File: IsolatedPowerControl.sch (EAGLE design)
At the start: 41 parts, among them Q1 FDN340P, Q2 FDN340P, U1 MCP23008-E/SO, U2 MCP4716A0T-E/CH, U3 MCP6273T-E/CH

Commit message: Another reroute!
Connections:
- net LOWSIDEONOFF_A: now also U1.GP7; no longer U1.GP1
- net V+: now also U1.GP1
- net V-: now also U1.GP5, U1.GP6
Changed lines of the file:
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@@
 <part name="R12" library="rcl" deviceset="R-EU_" device="R0603" value="10"/>
 <part name="P+9" library="supply1" deviceset="V+" device=""/>
-<part name="P-5" library="supply1" deviceset="V-" device=""/>
 <part name="U2" library="MCP4716A0T" deviceset="MCP4716A0T-E/CH" device=""/>
 <part name="P-6" library="supply1" deviceset="V-" device=""/>
@@
 <part name="R16" library="rcl" deviceset="R-EU_" device="R0805" value="10K"/>
 <part name="Q2" library="transistor-power" deviceset="FDN360P" device="" value="FDN340P"/>
+<part name="P-5" library="supply1" deviceset="V-" device=""/>
 </parts>
 <sheets>
@@
 <instance part="R12" gate="G$1" x="332.74" y="40.64" rot="R180"/>
 <instance part="P+9" gate="1" x="347.98" y="60.96"/>
-<instance part="P-5" gate="1" x="248.92" y="22.86"/>
 <instance part="U2" gate="A" x="213.36" y="-63.5"/>
 <instance part="P-6" gate="1" x="175.26" y="-81.28"/>
@@
 <instance part="R16" gate="G$1" x="340.36" y="12.7" rot="R90"/>
 <instance part="Q2" gate="G$1" x="345.44" y="2.54"/>
+<instance part="P-5" gate="1" x="248.92" y="-12.7"/>
 </instances>
 <busses>
@@
 <wire x1="248.92" y1="38.1" x2="248.92" y2="35.56" width="0.1524" layer="91"/>
 <pinref part="C2" gate="G$1" pin="1"/>
+<pinref part="U1" gate="A" pin="GP1"/>
+<wire x1="238.76" y1="5.08" x2="241.3" y2="5.08" width="0.1524" layer="91"/>
+<wire x1="241.3" y1="5.08" x2="241.3" y2="22.86" width="0.1524" layer="91"/>
+<junction x="241.3" y="22.86"/>
 </segment>
 <segment>
@@
 </segment>
 <segment>
-<pinref part="P-5" gate="1" pin="V-"/>
-<wire x1="248.92" y1="27.94" x2="248.92" y2="25.4" width="0.1524" layer="91"/>
-<pinref part="C2" gate="G$1" pin="2"/>
-</segment>
-<segment>
 <pinref part="U2" gate="A" pin="VSS"/>
 <wire x1="195.58" y1="-73.66" x2="175.26" y2="-73.66" width="0.1524" layer="91"/>
@@
 <wire x1="248.92" y1="-73.66" x2="248.92" y2="-76.2" width="0.1524" layer="91"/>
 <pinref part="P-10" gate="1" pin="V-"/>
+</segment>
+<segment>
+<pinref part="C2" gate="G$1" pin="2"/>
+<pinref part="U1" gate="A" pin="GP6"/>
+<wire x1="238.76" y1="17.78" x2="248.92" y2="17.78" width="0.1524" layer="91"/>
+<wire x1="248.92" y1="17.78" x2="248.92" y2="15.24" width="0.1524" layer="91"/>
+<pinref part="U1" gate="A" pin="GP5"/>
+<wire x1="248.92" y1="15.24" x2="238.76" y2="15.24" width="0.1524" layer="91"/>
+<wire x1="248.92" y1="15.24" x2="248.92" y2="-10.16" width="0.1524" layer="91"/>
+<junction x="248.92" y="15.24"/>
+<wire x1="248.92" y1="27.94" x2="248.92" y2="17.78" width="0.1524" layer="91"/>
+<junction x="248.92" y="17.78"/>
+<pinref part="P-5" gate="1" pin="V-"/>
 </segment>
 </net>
@@
 <net name="LOWSIDEONOFF_A" class="0">
 <segment>
-<pinref part="U1" gate="A" pin="GP1"/>
-<wire x1="238.76" y1="5.08" x2="269.24" y2="5.08" width="0.1524" layer="91"/>
-<label x="254" y="5.08" size="1.778" layer="95"/>
-</segment>
-<segment>
 <wire x1="302.26" y1="-22.86" x2="327.66" y2="-22.86" width="0.1524" layer="91"/>
 <label x="302.26" y="-22.86" size="1.778" layer="95"/>
 <pinref part="R11" gate="G$1" pin="1"/>
 </segment>
-</net>
+<segment>
+<pinref part="U1" gate="A" pin="GP7"/>
+<wire x1="238.76" y1="20.32" x2="269.24" y2="20.32" width="0.1524" layer="91"/>
+<label x="254" y="20.32" size="1.778" layer="95"/>
+</segment>
+</net>

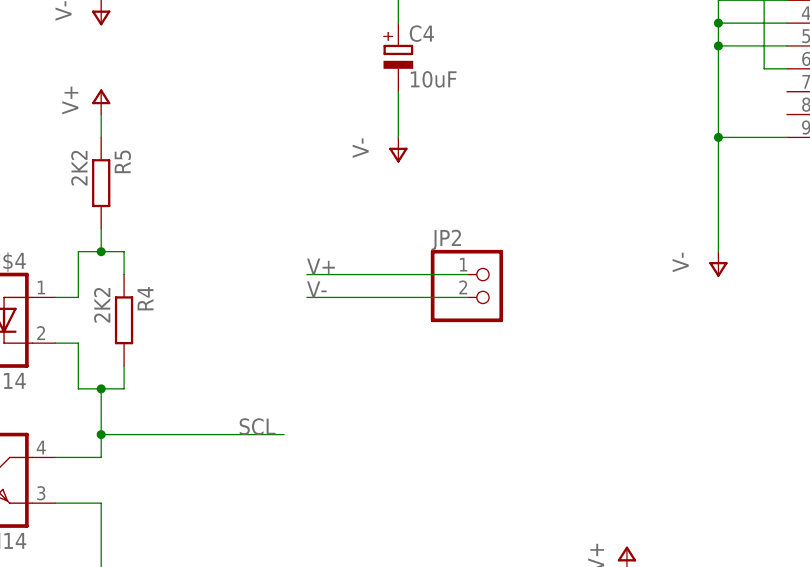
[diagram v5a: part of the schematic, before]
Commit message: Tweaks following etching to open up clearances
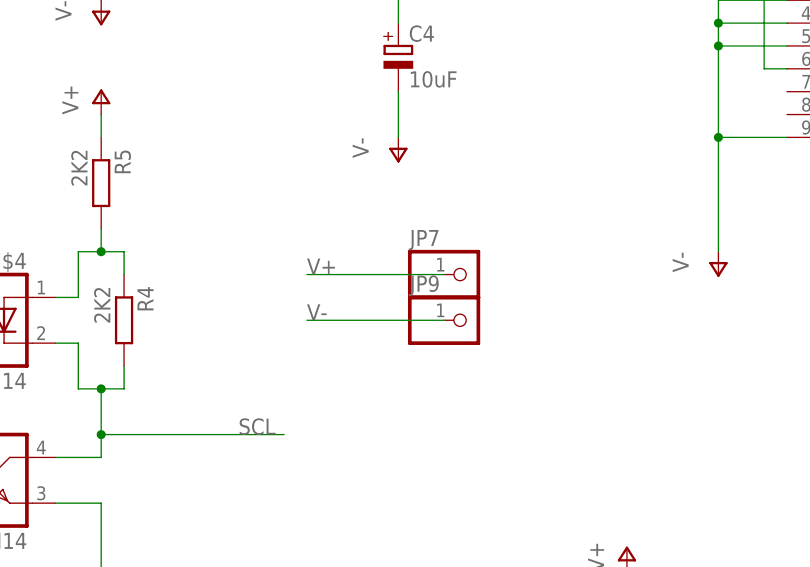
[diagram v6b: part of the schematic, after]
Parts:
- removed JP2: (no value), pinhead:PINHD-1X2
- added JP7, JP9: (no value), pinhead:PINHD-1X1LARGEPAD
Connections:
- net V+: now also JP7.1; no longer JP2.1
- net V-: now also JP9.1; no longer JP2.2
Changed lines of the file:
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@@
 <part name="GND5" library="supply1" deviceset="GND" device=""/>
 <part name="JP5" library="pinhead" deviceset="PINHD-1X4" device=""/>
-<part name="JP2" library="pinhead" deviceset="PINHD-1X2" device=""/>
 <part name="JP1" library="pinhead" deviceset="PINHD-1X1" device="LARGEPAD"/>
 <part name="JP3" library="pinhead" deviceset="PINHD-1X1" device="LARGEPAD"/>
@@
 <part name="Q2" library="transistor-power" deviceset="FDN360P" device="" value="FDN340P"/>
 <part name="P-5" library="supply1" deviceset="V-" device=""/>
+<part name="JP7" library="pinhead" deviceset="PINHD-1X1" device="LARGEPAD"/>
+<part name="JP9" library="pinhead" deviceset="PINHD-1X1" device="LARGEPAD"/>
 </parts>
 <sheets>
@@
 <instance part="GND5" gate="1" x="17.78" y="20.32"/>
 <instance part="JP5" gate="A" x="-88.9" y="12.7" rot="MR0"/>
-<instance part="JP2" gate="G$1" x="160.02" y="-15.24"/>
 <instance part="JP1" gate="G$1" x="449.58" y="25.4"/>
 <instance part="JP3" gate="G$1" x="449.58" y="30.48"/>
@@
 <instance part="Q2" gate="G$1" x="345.44" y="2.54"/>
 <instance part="P-5" gate="1" x="248.92" y="-12.7"/>
+<instance part="JP7" gate="G$1" x="157.48" y="-12.7"/>
+<instance part="JP9" gate="G$1" x="157.48" y="-17.78"/>
 </instances>
 <busses>
@@
 </segment>
 <segment>
-<wire x1="157.48" y1="-12.7" x2="139.7" y2="-12.7" width="0.1524" layer="91"/>
+<wire x1="154.94" y1="-12.7" x2="139.7" y2="-12.7" width="0.1524" layer="91"/>
 <label x="139.7" y="-12.7" size="1.778" layer="95"/>
-<pinref part="JP2" gate="G$1" pin="1"/>
+<pinref part="JP7" gate="G$1" pin="1"/>
 </segment>
 <segment>
@@
 </segment>
 <segment>
-<wire x1="157.48" y1="-15.24" x2="139.7" y2="-15.24" width="0.1524" layer="91"/>
-<label x="139.7" y="-15.24" size="1.778" layer="95"/>
-<pinref part="JP2" gate="G$1" pin="2"/>
-</segment>
-<segment>
+<wire x1="154.94" y1="-17.78" x2="139.7" y2="-17.78" width="0.1524" layer="91"/>
+<label x="139.7" y="-17.78" size="1.778" layer="95"/>
+<pinref part="JP9" gate="G$1" pin="1"/>
+</segment>
+<segment>

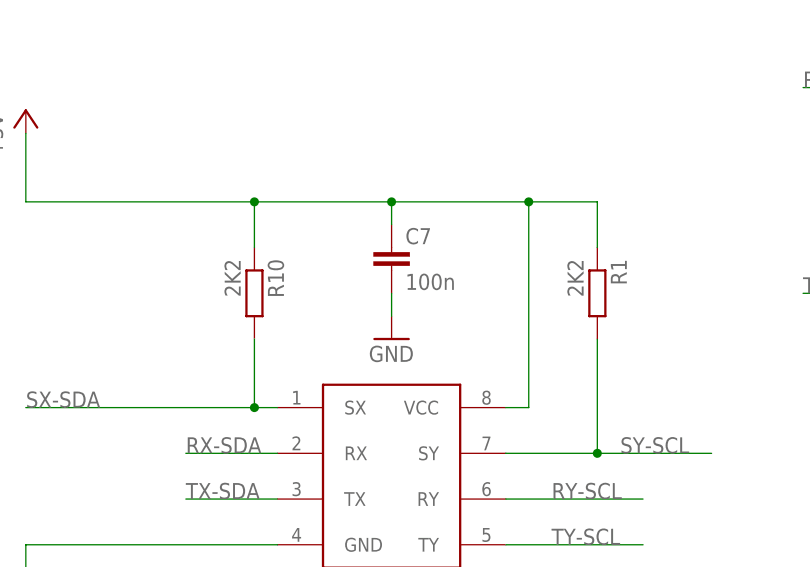
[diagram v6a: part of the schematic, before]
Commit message: Added test software
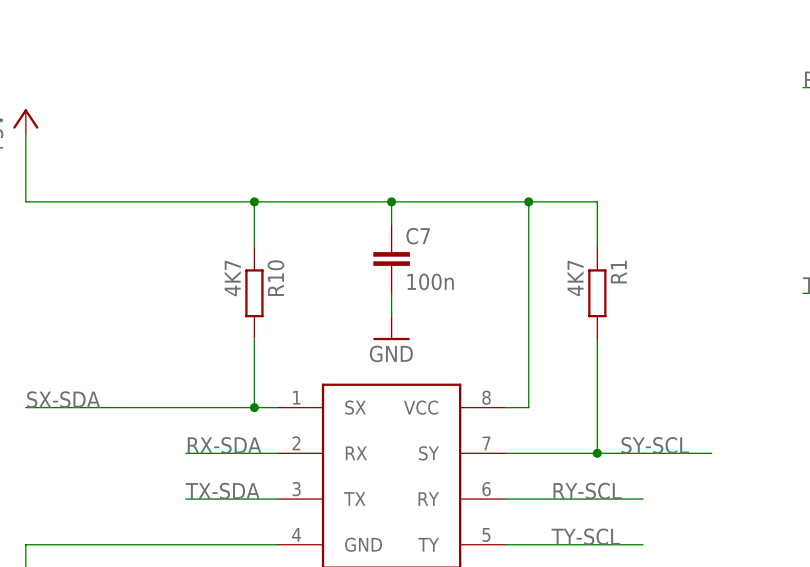
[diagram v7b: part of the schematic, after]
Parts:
- R1, R10: value 2K2 -> 4K7
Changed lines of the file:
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@@
 <grid distance="0.1" unitdist="inch" unit="inch" style="lines" multiple="1" display="no" altdistance="0.01" altunitdist="inch" altunit="inch"/>
 <layers>
-<layer number="1" name="Top" color="4" fill="1" visible="no" active="no"/>
-<layer number="2" name="Route2" color="1" fill="3" visible="no" active="no"/>
-<layer number="3" name="Route3" color="4" fill="3" visible="no" active="no"/>
-<layer number="14" name="Route14" color="1" fill="6" visible="no" active="no"/>
-<layer number="15" name="Route15" color="4" fill="6" visible="no" active="no"/>
-<layer number="16" name="Bottom" color="1" fill="1" visible="no" active="no"/>
-<layer number="17" name="Pads" color="2" fill="1" visible="no" active="no"/>
-<layer number="18" name="Vias" color="2" fill="1" visible="no" active="no"/>
-<layer number="19" name="Unrouted" color="6" fill="1" visible="no" active="no"/>
-<layer number="20" name="Dimension" color="15" fill="1" visible="no" active="no"/>
-<layer number="21" name="tPlace" color="7" fill="1" visible="no" active="no"/>
-<layer number="22" name="bPlace" color="7" fill="1" visible="no" active="no"/>
-<layer number="23" name="tOrigins" color="15" fill="1" visible="no" active="no"/>
-<layer number="24" name="bOrigins" color="15" fill="1" visible="no" active="no"/>
-<layer number="25" name="tNames" color="7" fill="1" visible="no" active="no"/>
-<layer number="26" name="bNames" color="7" fill="1" visible="no" active="no"/>
-<layer number="27" name="tValues" color="7" fill="1" visible="no" active="no"/>
-<layer number="28" name="bValues" color="7" fill="1" visible="no" active="no"/>
+<layer number="1" name="Top" color="4" fill="1" visible="yes" active="no"/>
+<layer number="2" name="Route2" color="1" fill="3" visible="yes" active="no"/>
+<layer number="3" name="Route3" color="4" fill="3" visible="yes" active="no"/>
+<layer number="14" name="Route14" color="1" fill="6" visible="yes" active="no"/>
+<layer number="15" name="Route15" color="4" fill="6" visible="yes" active="no"/>
+<layer number="16" name="Bottom" color="1" fill="1" visible="yes" active="no"/>
+<layer number="17" name="Pads" color="2" fill="1" visible="yes" active="no"/>
+<layer number="18" name="Vias" color="2" fill="1" visible="yes" active="no"/>
+<layer number="19" name="Unrouted" color="6" fill="1" visible="yes" active="no"/>
+<layer number="20" name="Dimension" color="15" fill="1" visible="yes" active="no"/>
+<layer number="21" name="tPlace" color="7" fill="1" visible="yes" active="no"/>
+<layer number="22" name="bPlace" color="7" fill="1" visible="yes" active="no"/>
+<layer number="23" name="tOrigins" color="15" fill="1" visible="yes" active="no"/>
+<layer number="24" name="bOrigins" color="15" fill="1" visible="yes" active="no"/>
+<layer number="25" name="tNames" color="7" fill="1" visible="yes" active="no"/>
+<layer number="26" name="bNames" color="7" fill="1" visible="yes" active="no"/>
+<layer number="27" name="tValues" color="7" fill="1" visible="yes" active="no"/>
+<layer number="28" name="bValues" color="7" fill="1" visible="yes" active="no"/>
 <layer number="29" name="tStop" color="7" fill="3" visible="no" active="no"/>
 <layer number="30" name="bStop" color="7" fill="6" visible="no" active="no"/>
@@
 <layer number="35" name="tGlue" color="7" fill="4" visible="no" active="no"/>
 <layer number="36" name="bGlue" color="7" fill="5" visible="no" active="no"/>
-<layer number="37" name="tTest" color="7" fill="1" visible="no" active="no"/>
-<layer number="38" name="bTest" color="7" fill="1" visible="no" active="no"/>
+<layer number="37" name="tTest" color="7" fill="1" visible="yes" active="no"/>
+<layer number="38" name="bTest" color="7" fill="1" visible="yes" active="no"/>
 <layer number="39" name="tKeepout" color="4" fill="11" visible="no" active="no"/>
 <layer number="40" name="bKeepout" color="1" fill="11" visible="no" active="no"/>
@@
 <layer number="44" name="Drills" color="7" fill="1" visible="no" active="no"/>
 <layer number="45" name="Holes" color="7" fill="1" visible="no" active="no"/>
-<layer number="46" name="Milling" color="3" fill="1" visible="no" active="no"/>
-<layer number="47" name="Measures" color="7" fill="1" visible="no" active="no"/>
-<layer number="48" name="Document" color="7" fill="1" visible="no" active="no"/>
-<layer number="49" name="Reference" color="7" fill="1" visible="no" active="no"/>
-<layer number="50" name="dxf" color="7" fill="1" visible="no" active="no"/>
-<layer number="51" name="tDocu" color="7" fill="1" visible="no" active="no"/>
-<layer number="52" name="bDocu" color="7" fill="1" visible="no" active="no"/>
-<layer number="53" name="tGND_GNDA" color="7" fill="9" visible="no" active="no"/>
-<layer number="54" name="bGND_GNDA" color="1" fill="9" visible="no" active="no"/>
-<layer number="56" name="wert" color="7" fill="1" visible="no" active="no"/>
+<layer number="46" name="Milling" color="3" fill="1" visible="yes" active="no"/>
+<layer number="47" name="Measures" color="7" fill="1" visible="yes" active="no"/>
+<layer number="48" name="Document" color="7" fill="1" visible="yes" active="no"/>
+<layer number="49" name="Reference" color="7" fill="1" visible="yes" active="no"/>
+<layer number="50" name="dxf" color="7" fill="1" visible="yes" active="no"/>
+<layer number="51" name="tDocu" color="7" fill="1" visible="yes" active="no"/>
+<layer number="52" name="bDocu" color="7" fill="1" visible="yes" active="no"/>
+<layer number="53" name="tGND_GNDA" color="7" fill="9" visible="yes" active="no"/>
+<layer number="54" name="bGND_GNDA" color="1" fill="9" visible="yes" active="no"/>
+<layer number="56" name="wert" color="7" fill="1" visible="yes" active="no"/>
 <layer number="90" name="Modules" color="5" fill="1" visible="yes" active="yes"/>
 <layer number="91" name="Nets" color="2" fill="1" visible="yes" active="yes"/>
@@
 <part name="C3" library="rcl" deviceset="C-EU" device="C1206K" value="100n"/>
 <part name="C6" library="rcl" deviceset="C-EU" device="C1206K" value="100n"/>
-<part name="R1" library="rcl" deviceset="R-EU_" device="R0402" value="2K2"/>
-<part name="R10" library="rcl" deviceset="R-EU_" device="R0402" value="2K2"/>
+<part name="R1" library="rcl" deviceset="R-EU_" device="R0402" value="4K7"/>
+<part name="R10" library="rcl" deviceset="R-EU_" device="R0402" value="4K7"/>
 <part name="Q1" library="transistor-power" deviceset="FDN360P" device="" value="FDN340P"/>
 <part name="C7" library="rcl" deviceset="C-EU" device="C1206K" value="100n"/>

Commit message: Added documentation to schematic. Added STM32 test sketch
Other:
- note added: "Din connection cable: - Power - Of red and black, red is +ve - Of white and black, black is -ve - Signals - Of red and black, black is SCL - Of white and black, black is SDA"
- moved on the sheet: C1, C3, C6, JP1, JP3, JP4, JP6, JP8, R13, U2, U3
